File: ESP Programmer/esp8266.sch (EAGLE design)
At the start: 11 parts

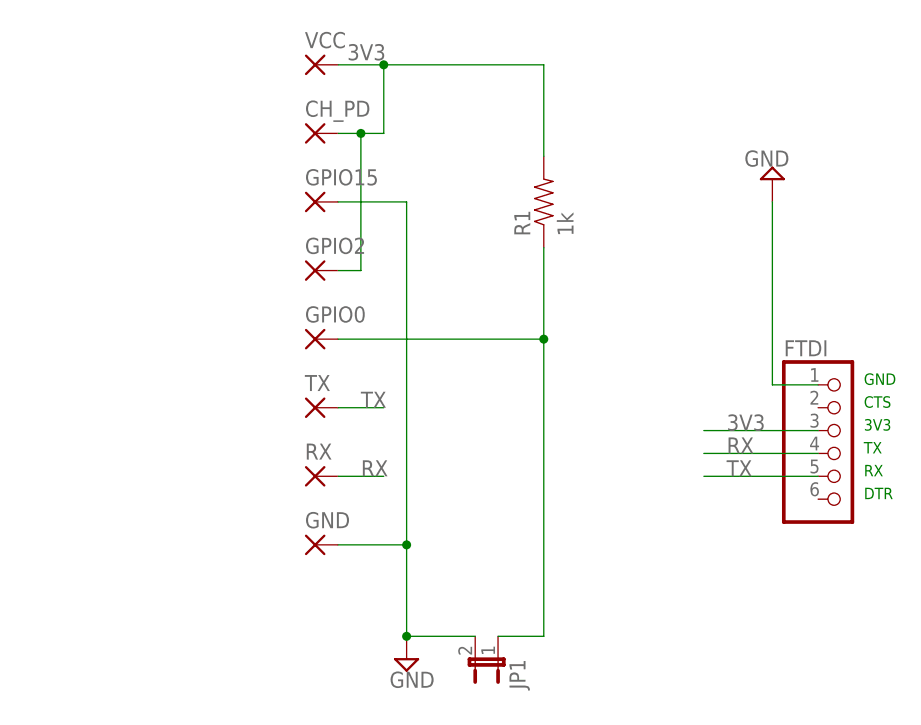
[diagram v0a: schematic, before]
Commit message: remove old dead projects, add esp-01 sensor stuff
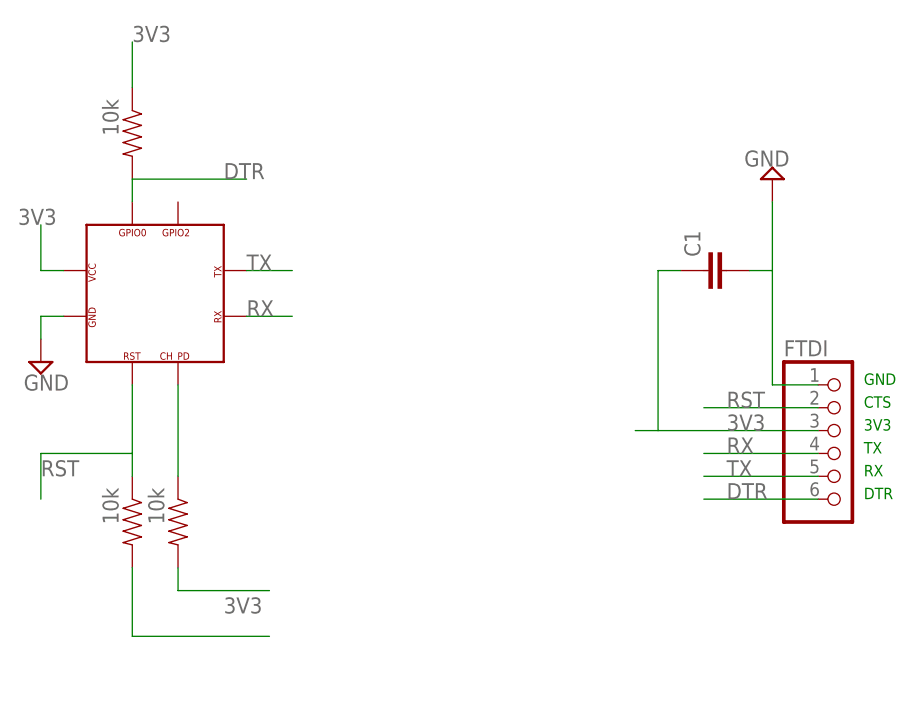
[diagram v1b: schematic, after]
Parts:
- removed CH_PD, GND, GPIO0, GPIO15, GPIO2, RX, TX, VCC: (no value), wirepad:1,6/0,9
- removed JP1: (no value), jumper:JP1E
- added C1: (no value), SparkFun-Capacitors:CAPEZ
- added R2, R3: 10k, SparkFun-Passives:RESISTORPTH-1/2W
- added U$1: ESP-01, Franc:ESP-01
- R1: value 1k -> 10k
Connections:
- removed net N$1: GPIO0.P, JP1.1, R1.1
- new net DTR: FTDI.6, R1.2, U$1.GPIO0
- new net N$3: R2.1, U$1.CP_PD
- new net RST: FTDI.2, R3.1, U$1.RST
- net 3V3: now also C1.1, R1.1, R2.2, R3.2, U$1.VCC; no longer CH_PD.P, GPIO2.P, R1.2, VCC.P
- net GND: now also C1.2, U$1.GND; no longer GND.P, GPIO15.P, JP1.2
- net RX: now also U$1.RX; no longer RX.P
- net TX: now also U$1.TX; no longer TX.P
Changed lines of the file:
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@@
 </classes>
 <parts>
-<part name="VCC" library="wirepad" deviceset="1,6/0,9" device=""/>
-<part name="CH_PD" library="wirepad" deviceset="1,6/0,9" device=""/>
-<part name="GPIO15" library="wirepad" deviceset="1,6/0,9" device=""/>
-<part name="GPIO2" library="wirepad" deviceset="1,6/0,9" device=""/>
-<part name="GPIO0" library="wirepad" deviceset="1,6/0,9" device=""/>
-<part name="TX" library="wirepad" deviceset="1,6/0,9" device=""/>
-<part name="RX" library="wirepad" deviceset="1,6/0,9" device=""/>
-<part name="GND" library="wirepad" deviceset="1,6/0,9" device=""/>
 <part name="SUPPLY1" library="supply2" deviceset="GND" device=""/>
-<part name="JP1" library="jumper" deviceset="JP1E" device=""/>
-<part name="R1" library="SparkFun-Passives" deviceset="RESISTOR" device="PTH-1/2W" value="1k"/>
 <part name="FTDI" library="pinhead" deviceset="PINHD-1X6" device="/90"/>
 <part name="SUPPLY2" library="supply2" deviceset="GND" device=""/>
+<part name="U$1" library="Franc" deviceset="ESP-01" device=""/>
+<part name="R3" library="SparkFun-Passives" deviceset="RESISTOR" device="PTH-1/2W" value="10k"/>
+<part name="R1" library="SparkFun-Passives" deviceset="RESISTOR" device="PTH-1/2W" value="10k"/>
+<part name="R2" library="SparkFun-Passives" deviceset="RESISTOR" device="PTH-1/2W" value="10k"/>
+<part name="C1" library="SparkFun-Capacitors" deviceset="CAP" device="EZ"/>
 </parts>
 <sheets>
@@
 </plain>
 <instances>
-<instance part="VCC" gate="1" x="-12.7" y="78.74"/>
-<instance part="CH_PD" gate="1" x="-12.7" y="71.12"/>
-<instance part="GPIO15" gate="1" x="-12.7" y="63.5"/>
-<instance part="GPIO2" gate="1" x="-12.7" y="55.88"/>
-<instance part="GPIO0" gate="1" x="-12.7" y="48.26"/>
-<instance part="TX" gate="1" x="-12.7" y="40.64"/>
-<instance part="RX" gate="1" x="-12.7" y="33.02"/>
-<instance part="GND" gate="1" x="-12.7" y="25.4"/>
-<instance part="SUPPLY1" gate="GND" x="-2.54" y="12.7"/>
-<instance part="JP1" gate="A" x="7.62" y="12.7" rot="R180"/>
-<instance part="R1" gate="G$1" x="12.7" y="63.5" rot="R90"/>
+<instance part="SUPPLY1" gate="GND" x="-43.18" y="45.72"/>
 <instance part="FTDI" gate="A" x="45.72" y="35.56"/>
 <instance part="SUPPLY2" gate="GND" x="38.1" y="66.04" rot="R180"/>
+<instance part="U$1" gate="G$1" x="-30.48" y="53.34"/>
+<instance part="R3" gate="G$1" x="-33.02" y="27.94" smashed="yes" rot="R270">
+<attribute name="VALUE" x="-36.322" y="31.75" size="1.778" layer="96" rot="R270"/>
+</instance>
+<instance part="R1" gate="G$1" x="-33.02" y="71.12" smashed="yes" rot="R270">
+<attribute name="VALUE" x="-36.322" y="74.93" size="1.778" layer="96" rot="R270"/>
+</instance>
+<instance part="R2" gate="G$1" x="-27.94" y="27.94" smashed="yes" rot="R270">
+<attribute name="VALUE" x="-31.242" y="31.75" size="1.778" layer="96" rot="R270"/>
+</instance>
+<instance part="C1" gate="G$1" x="33.02" y="55.88" rot="R90"/>
 </instances>
 <busses>
@@
 <segment>
 <pinref part="SUPPLY1" gate="GND" pin="GND"/>
-<pinref part="GND" gate="1" pin="P"/>
-<wire x1="-2.54" y1="25.4" x2="-2.54" y2="15.24" width="0.1524" layer="91"/>
-<wire x1="-10.16" y1="25.4" x2="-2.54" y2="25.4" width="0.1524" layer="91"/>
-<pinref part="GPIO15" gate="1" pin="P"/>
-<wire x1="-10.16" y1="63.5" x2="-2.54" y2="63.5" width="0.1524" layer="91"/>
-<wire x1="-2.54" y1="63.5" x2="-2.54" y2="25.4" width="0.1524" layer="91"/>
-<junction x="-2.54" y="25.4"/>
-<pinref part="JP1" gate="A" pin="2"/>
-<wire x1="5.08" y1="15.24" x2="-2.54" y2="15.24" width="0.1524" layer="91"/>
-<junction x="-2.54" y="15.24"/>
+<pinref part="U$1" gate="G$1" pin="GND"/>
+<wire x1="-43.18" y1="48.26" x2="-43.18" y2="50.8" width="0.1524" layer="91"/>
+<wire x1="-43.18" y1="50.8" x2="-40.64" y2="50.8" width="0.1524" layer="91"/>
 </segment>
 <segment>
@@
 <wire x1="43.18" y1="43.18" x2="38.1" y2="43.18" width="0.1524" layer="91"/>
 <pinref part="SUPPLY2" gate="GND" pin="GND"/>
-<wire x1="38.1" y1="63.5" x2="38.1" y2="43.18" width="0.1524" layer="91"/>
+<wire x1="38.1" y1="63.5" x2="38.1" y2="55.88" width="0.1524" layer="91"/>
+<pinref part="C1" gate="G$1" pin="2"/>
+<wire x1="38.1" y1="55.88" x2="38.1" y2="43.18" width="0.1524" layer="91"/>
+<wire x1="35.56" y1="55.88" x2="38.1" y2="55.88" width="0.1524" layer="91"/>
 </segment>
 </net>
@@
 <segment>
 <pinref part="FTDI" gate="A" pin="3"/>
-<wire x1="43.18" y1="38.1" x2="30.48" y2="38.1" width="0.1524" layer="91"/>
+<wire x1="43.18" y1="38.1" x2="25.4" y2="38.1" width="0.1524" layer="91"/>
 <label x="33.02" y="38.1" size="1.778" layer="95"/>
+<pinref part="C1" gate="G$1" pin="1"/>
+<wire x1="25.4" y1="38.1" x2="22.86" y2="38.1" width="0.1524" layer="91"/>
+<wire x1="27.94" y1="55.88" x2="25.4" y2="55.88" width="0.1524" layer="91"/>
+<wire x1="25.4" y1="55.88" x2="25.4" y2="38.1" width="0.1524" layer="91"/>
 </segment>
 <segment>
-<pinref part="VCC" gate="1" pin="P"/>
-<wire x1="-10.16" y1="78.74" x2="-5.08" y2="78.74" width="0.1524" layer="91"/>
-<pinref part="CH_PD" gate="1" pin="P"/>
-<wire x1="-10.16" y1="71.12" x2="-7.62" y2="71.12" width="0.1524" layer="91"/>
-<wire x1="-7.62" y1="71.12" x2="-5.08" y2="71.12" width="0.1524" layer="91"/>
-<wire x1="-5.08" y1="71.12" x2="-5.08" y2="78.74" width="0.1524" layer="91"/>
-<pinref part="GPIO2" gate="1" pin="P"/>
-<wire x1="-10.16" y1="55.88" x2="-7.62" y2="55.88" width="0.1524" layer="91"/>
-<wire x1="-7.62" y1="55.88" x2="-7.62" y2="71.12" width="0.1524" layer="91"/>
-<junction x="-7.62" y="71.12"/>
-<junction x="-5.08" y="78.74"/>
-<pinref part="R1" gate="G$1" pin="2"/>
-<wire x1="12.7" y1="68.58" x2="12.7" y2="78.74" width="0.1524" layer="91"/>
-<wire x1="12.7" y1="78.74" x2="-5.08" y2="78.74" width="0.1524" layer="91"/>
-<label x="-9.144" y="79.248" size="1.778" layer="95"/>
+<wire x1="-33.02" y1="76.2" x2="-33.02" y2="81.28" width="0.1524" layer="91"/>
+<label x="-33.02" y="81.28" size="1.778" layer="95"/>
+<pinref part="R1" gate="G$1" pin="1"/>
+</segment>
+<segment>
+<pinref part="R2" gate="G$1" pin="2"/>
+<wire x1="-27.94" y1="20.32" x2="-17.78" y2="20.32" width="0.1524" layer="91"/>
+<wire x1="-27.94" y1="22.86" x2="-27.94" y2="20.32" width="0.1524" layer="91"/>
+<label x="-22.86" y="17.78" size="1.778" layer="95"/>
+</segment>
+<segment>
+<pinref part="U$1" gate="G$1" pin="VCC"/>
+<wire x1="-40.64" y1="55.88" x2="-43.18" y2="55.88" width="0.1524" layer="91"/>
+<wire x1="-43.18" y1="55.88" x2="-43.18" y2="60.96" width="0.1524" layer="91"/>
+<label x="-45.72" y="60.96" size="1.778" layer="95"/>
+</segment>
+<segment>
+<pinref part="R3" gate="G$1" pin="2"/>
+<wire x1="-33.02" y1="22.86" x2="-33.02" y2="15.24" width="0.1524" layer="91"/>
+<wire x1="-33.02" y1="15.24" x2="-17.78" y2="15.24" width="0.1524" layer="91"/>
 </segment>
 </net>
 <net name="TX" class="0">
 <segment>
-<pinref part="TX" gate="1" pin="P"/>
-<wire x1="-10.16" y1="40.64" x2="-5.08" y2="40.64" width="0.1524" layer="91"/>
-<label x="-7.62" y="40.64" size="1.778" layer="95"/>
+<label x="-20.32" y="55.88" size="1.778" layer="95"/>
+<pinref part="U$1" gate="G$1" pin="TX"/>
+<wire x1="-15.24" y1="55.88" x2="-20.32" y2="55.88" width="0.1524" layer="91"/>
 </segment>
 <segment>
@@
 <wire x1="30.48" y1="33.02" x2="43.18" y2="33.02" width="0.1524" layer="91"/>
 <label x="33.02" y="33.02" size="1.778" layer="95"/>
-</segment>
-</net>
-<net name="N$1" class="0">
-<segment>
-<pinref part="GPIO0" gate="1" pin="P"/>
-<wire x1="-10.16" y1="48.26" x2="12.7" y2="48.26" width="0.1524" layer="91"/>
-<pinref part="R1" gate="G$1" pin="1"/>
-<wire x1="12.7" y1="48.26" x2="12.7" y2="58.42" width="0.1524" layer="91"/>
-<pinref part="JP1" gate="A" pin="1"/>
-<wire x1="12.7" y1="48.26" x2="12.7" y2="15.24" width="0.1524" layer="91"/>
-<wire x1="12.7" y1="15.24" x2="7.62" y2="15.24" width="0.1524" layer="91"/>
-<junction x="12.7" y="48.26"/>
 </segment>
 </net>
@@
 </segment>
 <segment>
-<pinref part="RX" gate="1" pin="P"/>
-<wire x1="-10.16" y1="33.02" x2="-5.08" y2="33.02" width="0.1524" layer="91"/>
-<label x="-7.62" y="33.02" size="1.778" layer="95"/>
+<wire x1="-15.24" y1="50.8" x2="-20.32" y2="50.8" width="0.1524" layer="91"/>
+<label x="-20.32" y="50.8" size="1.778" layer="95"/>
+<pinref part="U$1" gate="G$1" pin="RX"/>
 </segment>
 </net>
+<net name="RST" class="0">
+<segment>
+<pinref part="FTDI" gate="A" pin="2"/>
+<wire x1="43.18" y1="40.64" x2="30.48" y2="40.64" width="0.1524" layer="91"/>
+<label x="33.02" y="40.64" size="1.778" layer="95"/>
+</segment>
+<segment>
+<pinref part="U$1" gate="G$1" pin="RST"/>
+<pinref part="R3" gate="G$1" pin="1"/>
+<wire x1="-33.02" y1="43.18" x2="-33.02" y2="35.56" width="0.1524" layer="91"/>
+<wire x1="-33.02" y1="35.56" x2="-33.02" y2="33.02" width="0.1524" layer="91"/>
+<wire x1="-33.02" y1="35.56" x2="-43.18" y2="35.56" width="0.1524" layer="91"/>
+<wire x1="-43.18" y1="35.56" x2="-43.18" y2="30.48" width="0.1524" layer="91"/>
+<label x="-43.18" y="33.02" size="1.778" layer="95"/>
+</segment>
+</net>
+<net name="DTR" class="0">
+<segment>
+<pinref part="FTDI" gate="A" pin="6"/>
+<wire x1="43.18" y1="30.48" x2="30.48" y2="30.48" width="0.1524" layer="91"/>
+<label x="33.02" y="30.48" size="1.778" layer="95"/>
+</segment>
+<segment>
+<wire x1="-33.02" y1="63.5" x2="-33.02" y2="66.04" width="0.1524" layer="91"/>
+<pinref part="U$1" gate="G$1" pin="GPIO0"/>
+<pinref part="R1" gate="G$1" pin="2"/>
+<wire x1="-33.02" y1="66.04" x2="-20.32" y2="66.04" width="0.1524" layer="91"/>
+<label x="-22.86" y="66.04" size="1.778" layer="95"/>
+</segment>
+</net>
+<net name="N$3" class="0">
+<segment>
+<pinref part="U$1" gate="G$1" pin="CP_PD"/>
+<pinref part="R2" gate="G$1" pin="1"/>
+<wire x1="-27.94" y1="43.18" x2="-27.94" y2="33.02" width="0.1524" layer="91"/>
+</segment>
+</net>
